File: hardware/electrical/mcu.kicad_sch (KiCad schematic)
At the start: 38 parts, among them J2 STDC14, SW1 SW_Push, SW2 SW_Push, U8 STM32F446VET6, Y1 X322516MLB4SI, Y2 Q13FC1350000400

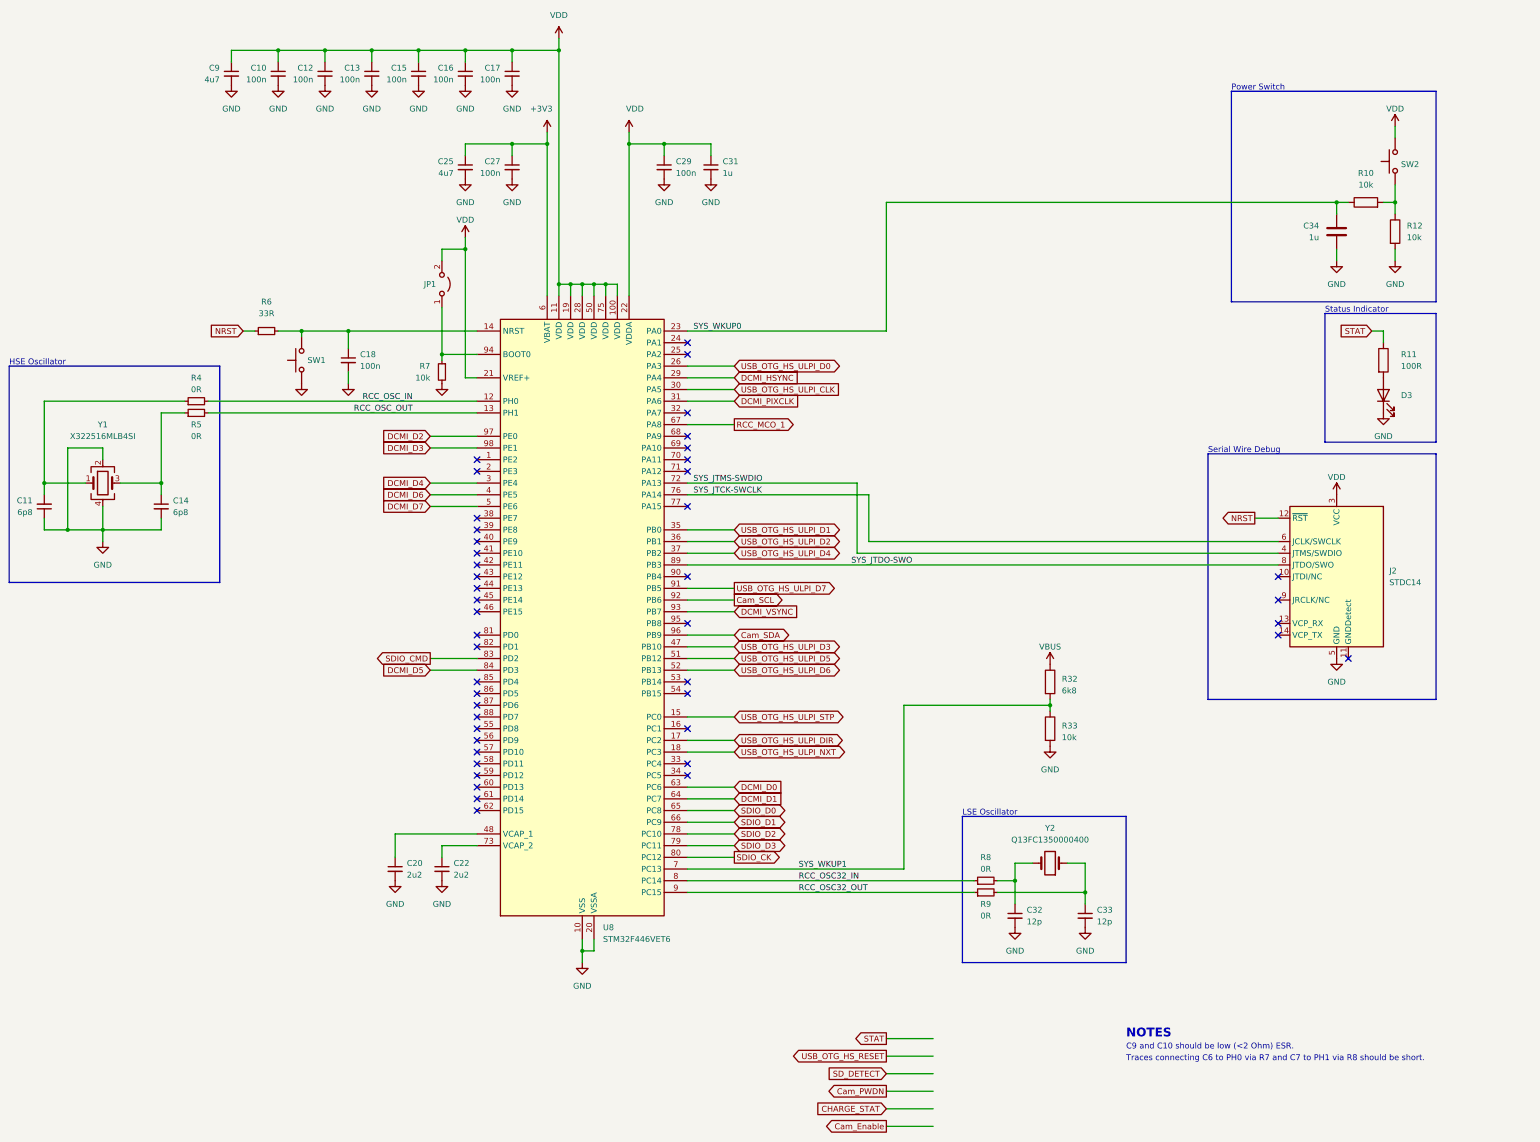
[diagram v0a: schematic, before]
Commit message: Replace Y1 and Y2 with generic crystals
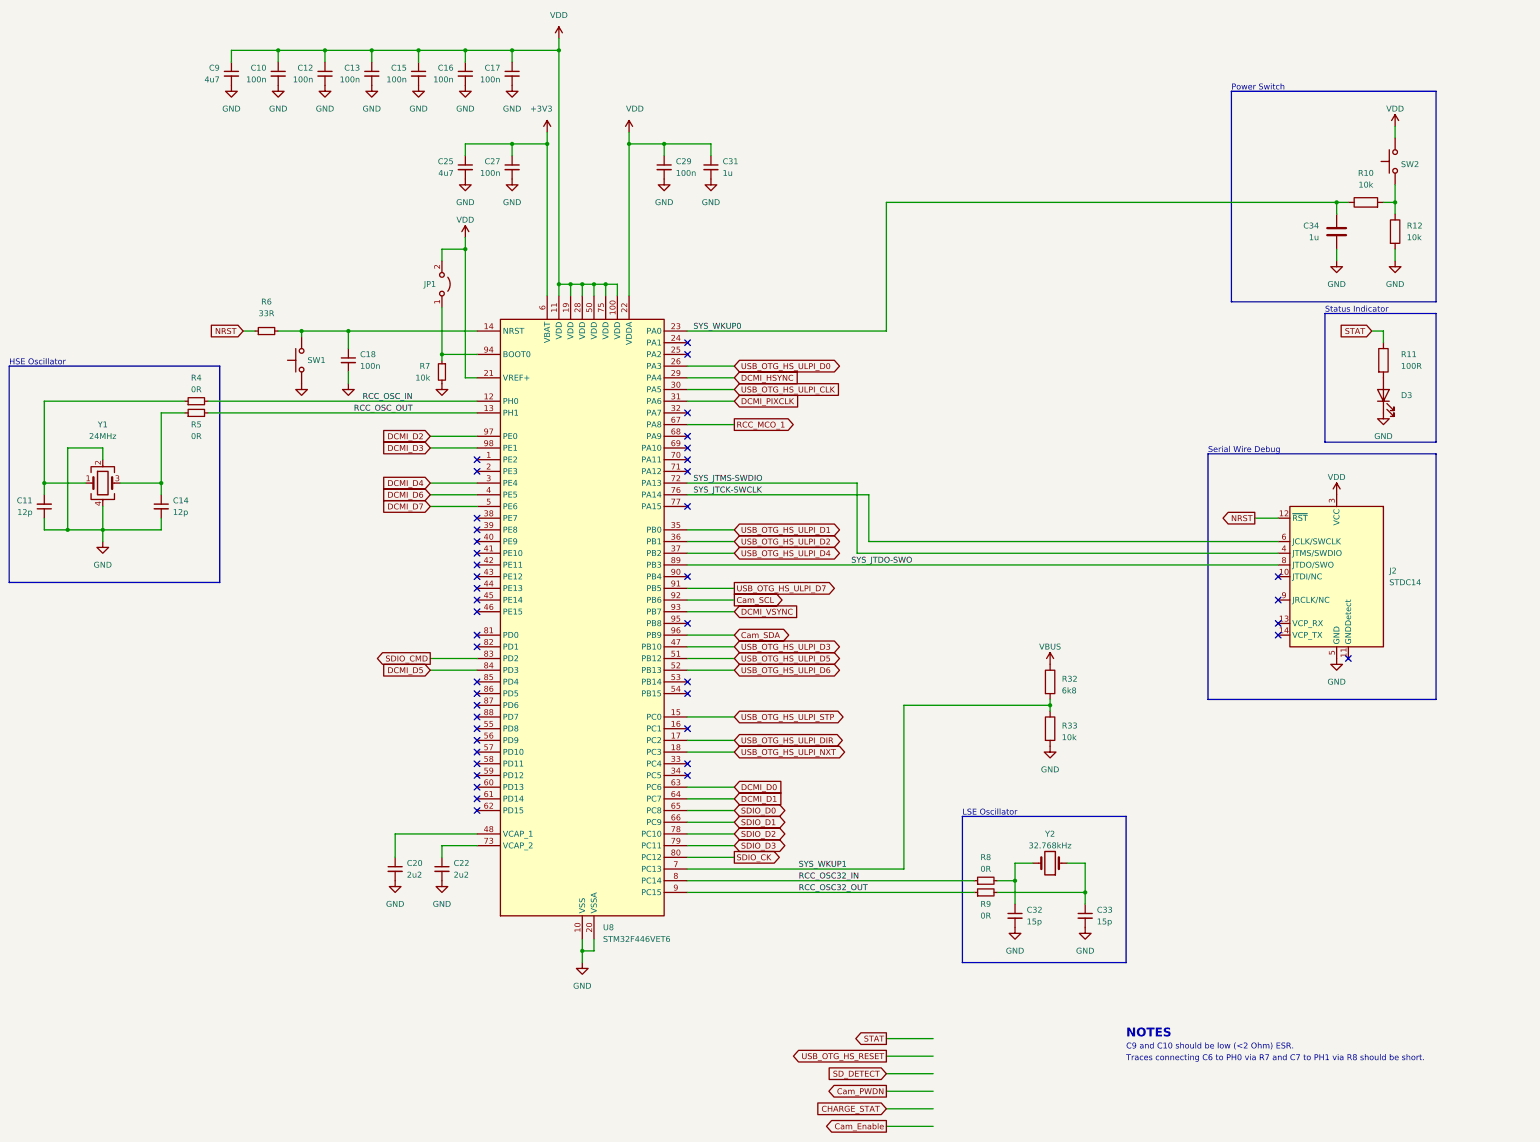
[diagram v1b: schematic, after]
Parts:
- C11, C14: value 6p8 -> 12p
- C32, C33: value 12p -> 15p
- Y1: value X322516MLB4SI -> 24MHz
- Y2: value Q13FC1350000400 -> 32.768kHz
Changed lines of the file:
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@@
   (symbol (lib_id "Device:Crystal") (at 283.21 209.55 180) (unit 1)
     (in_bom yes) (on_board yes) (dnp no) (fields_autoplaced)
-    (property "Reference" "Y2" (at 283.21 201.93 0)
-      (effects (font (size 1.27 1.27)))
-    )
-    (property "Value" "Q13FC1350000400" (at 283.21 204.47 0)
+    (property "Reference" "Y2" (at 283.21 203.2 0)
+      (effects (font (size 1.27 1.27)))
+    )
+    (property "Value" "32.768kHz" (at 283.21 205.74 0)
       (effects (font (size 1.27 1.27)))
     )
@@
   )
   (symbol (lib_id "Device:C_Small") (at 64.77 132.08 0) (mirror x) (unit 1)
-    (in_bom yes) (on_board yes) (dnp no) (fields_autoplaced)
-    (property "Reference" "C11" (at 62.23 130.8035 0)
+    (in_bom yes) (on_board yes) (dnp no)
+    (property "Reference" "C11" (at 62.23 130.81 0)
       (effects (font (size 1.27 1.27)) (justify right))
     )
-    (property "Value" "6p8" (at 62.23 133.3435 0)
+    (property "Value" "12p" (at 62.23 133.35 0)
       (effects (font (size 1.27 1.27)) (justify right))
     )
@@
       (effects (font (size 1.27 1.27)))
     )
-    (property "Value" "X322516MLB4SI" (at 77.47 116.84 0)
+    (property "Value" "24MHz" (at 77.47 116.84 0)
       (effects (font (size 1.27 1.27)))
     )
@@
   )
   (symbol (lib_id "Device:C_Small") (at 90.17 132.08 0) (unit 1)
-    (in_bom yes) (on_board yes) (dnp no) (fields_autoplaced)
-    (property "Reference" "C14" (at 92.71 130.8162 0)
-      (effects (font (size 1.27 1.27)) (justify left))
-    )
-    (property "Value" "6p8" (at 92.71 133.3562 0)
+    (in_bom yes) (on_board yes) (dnp no)
+    (property "Reference" "C14" (at 92.71 130.81 0)
+      (effects (font (size 1.27 1.27)) (justify left))
+    )
+    (property "Value" "12p" (at 92.71 133.35 0)
       (effects (font (size 1.27 1.27)) (justify left))
     )
@@
       (effects (font (size 1.27 1.27)) (justify left))
     )
-    (property "Value" "12p" (at 293.37 222.2562 0)
+    (property "Value" "15p" (at 293.37 222.2562 0)
       (effects (font (size 1.27 1.27)) (justify left))
     )
@@
       (effects (font (size 1.27 1.27)) (justify left))
     )
-    (property "Value" "12p" (at 278.13 222.2562 0)
-      (effects (font (size 1.27 1.27)) (justify left))
-    )
+    (property "Value" "15p" (at 278.13 222.2562 0)
+      (effects (font (size 1.27 1.27)) (justify left))
+    )

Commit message: Component selection
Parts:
- removed J2: STDC14, symbol Connector:Conn_ST_STDC14
- added J2: TC2030, Connector:Tag-Connect_TC2030-IDC-FP_2x03_P1.27mm_Vertical, symbol Connector:Conn_ARM_SWD_TagConnect_TC2030
- added Q8: 2N7002, Package_TO_SOT_SMD:SOT-23, symbol Transistor_FET:2N7002
- added R21: 100R, Resistor_SMD:R_0402_1005Metric, symbol Device:R
- C10, C12, C13, C15, C16, C17, C18, C27, C29: footprint (none) -> Capacitor_SMD:C_0402_1005Metric; LCSC Part # (none) -> C1525; Mfr (none) -> Samsung Electro-Mechanics; Mfr. Part # (none) -> CL05B104KO5NNNC
- C11, C14: footprint (none) -> Capacitor_SMD:C_0603_1608Metric; LCSC Part # (none) -> C38523; Mfr (none) -> Samsung Electro-Mechanics; Mfr. Part # (none) -> CL10C120JB8NNNC
- C20, C22: footprint (none) -> Capacitor_SMD:C_0402_1005Metric; LCSC Part # (none) -> C12530; Mfr (none) -> Samsung Electro-Mechanics; Mfr. Part # (none) -> CL05A225MQ5NSNC
- C25, C9: footprint (none) -> Capacitor_SMD:C_0402_1005Metric; LCSC Part # (none) -> C23733; Mfr (none) -> Samsung Electro-Mechanics; Mfr. Part # (none) -> CL05A475MP5NRNC
- C31, C34: footprint (none) -> Capacitor_SMD:C_0402_1005Metric; LCSC Part # (none) -> C52923; Mfr (none) -> Samsung Electro-Mechanics; Mfr. Part # (none) -> CL05A105KA5NQNC
- C32, C33: footprint (none) -> Capacitor_SMD:C_0603_1608Metric; LCSC Part # (none) -> C1644; Mfr (none) -> Samsung Electro-Mechanics; Mfr. Part # (none) -> CL10C150JB8NNNC
- D3: value LED -> RED; LCSC Part # (none) -> C131288; Mfr (none) -> Everlight Elec; Mfr. Part # (none) -> 12-21SURC/S530-A3/TR8
- JP1: now left out of the parts list
- R10, R12, R33, R7: footprint (none) -> Resistor_SMD:R_0402_1005Metric; LCSC Part # (none) -> C25744; Mfr (none) -> UNI-ROYAL(Uniroyal Elec); Mfr. Part # (none) -> 0402WGF1002TCE
- R11: value 100R -> 68R; footprint (none) -> Resistor_SMD:R_0603_1608Metric; LCSC Part # (none) -> C27592; Mfr (none) -> UNI-ROYAL(Uniroyal Elec); Mfr. Part # (none) -> 0603WAF680JT5E
- R32: footprint (none) -> Resistor_SMD:R_0402_1005Metric; LCSC Part # (none) -> C25917; Mfr (none) -> UNI-ROYAL(Uniroyal Elec); Mfr. Part # (none) -> 0402WGF6801TCE
- R4, R5, R8, R9: footprint (none) -> Resistor_SMD:R_0603_1608Metric_Pad0.98x0.95mm_HandSolder; LCSC Part # (none) -> C21189; Mfr (none) -> UNI-ROYAL(Uniroyal Elec); Mfr. Part # (none) -> 0603WAF0000T5E
- R6: footprint (none) -> Resistor_SMD:R_0402_1005Metric; LCSC Part # (none) -> C25105; Mfr (none) -> UNI-ROYAL(Uniroyal Elec); Mfr. Part # (none) -> 0402WGF330JTCE
- SW1: value SW_Push -> TS-1187A-B-A-B; LCSC Part # (none) -> C318884; Mfr (none) -> XKB Connectivity; Mfr. Part # (none) -> TS-1187A-B-A-B
- SW2: value SW_Push -> EVQP7C01K; LCSC Part # (none) -> C528965; Mfr (none) -> PANASONIC; Mfr. Part # (none) -> EVQP7C01K
- U8: LCSC Part # (none) -> C91929; Mfr (none) -> STMicroelectronics; Mfr. Part # (none) -> STM32F446VET6
- Y1: footprint (none) -> Crystal:Crystal_SMD_SeikoEpson_TSX3225-4Pin_3.2x2.5mm; LCSC Part # (none) -> C255917; Mfr (none) -> Seiko Epson; Mfr. Part # (none) -> X1E0000210129
- Y2: footprint (none) -> Crystal:Crystal_SMD_3215-2Pin_3.2x1.5mm; LCSC Part # (none) -> C32346; Mfr (none) -> Seiko Epson; Mfr. Part # (none) -> Q13FC1350000400
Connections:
- net GND: now also J2.5 (GND), Q8.3 (D); no longer D3.1 (K)
- net NRST: now also J2.3 (~{RESET})
- net STAT: now also R21.1; no longer R11.1
- net SYS_JTCK-SWCLK: now also J2.4 (SWCLK)
- net SYS_JTDO-SWO: now also J2.6 (SWO)
- net SYS_JTMS-SWDIO: now also J2.2 (SWDIO)
- net VDD: now also D3.2 (A), J2.1 (VCC)
- net at R11.2: now also Q8.2 (S); no longer D3.2 (A)
- new net: D3.1 (K), R11.1
- new net: Q8.1 (G), R21.2
- no-connect marks 45 -> 40
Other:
- moved on the sheet: D3, R11

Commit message: Add Everlight 12-21S footprint
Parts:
- D3: footprint (none) -> 3885:Everlight_21-21S
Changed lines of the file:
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@@
       (effects (font (size 1.27 1.27)) (justify right))
     )
-    (property "Footprint" "" (at 304.8 91.44 0)
+    (property "Footprint" "3885:Everlight_21-21S" (at 304.8 91.44 0)
       (effects (font (size 1.27 1.27)) hide)
     )

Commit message: Add Jushou AFC07-S24ECA-00 footprint and reverse J5 numbering to match camera cable
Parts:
- JP1: footprint (none) -> Jumper:SolderJumper-2_P1.3mm_Open_Pad1.0x1.5mm
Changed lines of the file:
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@@
       (effects (font (size 1.27 1.27)) (justify right) hide)
     )
-    (property "Footprint" "" (at 151.13 83.82 0)
+    (property "Footprint" "Jumper:SolderJumper-2_P1.3mm_Open_Pad1.0x1.5mm" (at 151.13 83.82 0)
       (effects (font (size 1.27 1.27)) hide)
     )

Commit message: Add footprint for XKB TS-1187A
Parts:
- SW1: footprint (none) -> 3885:SW_SPST_XKB_TS-1187A
- SW2: footprint (none) -> Button_Switch_SMD:SW_SPST_EVQP7C
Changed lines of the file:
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@@
       (effects (font (size 1.27 1.27)) (justify right) hide)
     )
-    (property "Footprint" "" (at 353.06 57.15 0)
+    (property "Footprint" "Button_Switch_SMD:SW_SPST_EVQP7C" (at 353.06 57.15 0)
       (effects (font (size 1.27 1.27)) hide)
     )
@@
       (effects (font (size 1.27 1.27)) (justify right) hide)
     )
-    (property "Footprint" "" (at 115.57 100.33 0)
-      (effects (font (size 1.27 1.27)) hide)
-    )
+    (property "Footprint" "3885:SW_SPST_XKB_TS-1187A" (at 115.57 100.33 0)
+      (effects (font (size 1.27 1.27)) hide)
+    )

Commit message: Route ULPI and power supply
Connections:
- net USB_OTG_HS_RESET: now also U8.2 (PE3)
- no-connect marks 40 -> 39
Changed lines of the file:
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@@
   (no_connect (at 204.47 170.18))
   (no_connect (at 158.75 182.88))
+  (no_connect (at 158.75 121.92))
   (no_connect (at 158.75 144.78))
-  (no_connect (at 158.75 121.92))
   (no_connect (at 158.75 147.32))
   (no_connect (at 204.47 121.92))
@@
   (no_connect (at 204.47 172.72))
   (no_connect (at 204.47 187.96))
-  (no_connect (at 158.75 124.46))
   (no_connect (at 204.47 99.06))
   (no_connect (at 158.75 137.16))
@@
     (stroke (width 0) (type default))
   )
-  (wire (pts (xy 257.81 251.46) (xy 247.65 251.46))
+  (wire (pts (xy 158.75 124.46) (xy 148.59 124.46))
     (stroke (width 0) (type default))
   )
@@
     )
   )
-  (global_label "USB_OTG_HS_RESET" (shape output) (at 247.65 251.46 180) (fields_autoplaced)
+  (global_label "USB_OTG_HS_RESET" (shape output) (at 148.59 124.46 180) (fields_autoplaced)
     (effects (font (size 1.27 1.27)) (justify right))
-    (property "Intersheetrefs" "${INTERSHEET_REFS}" (at 226.1782 251.46 0)
+    (property "Intersheetrefs" "${INTERSHEET_REFS}" (at 127.1182 124.46 0)
       (effects (font (size 1.27 1.27)) (justify right) hide)
     )
